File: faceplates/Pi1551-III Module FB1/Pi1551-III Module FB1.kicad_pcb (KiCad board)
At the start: 2 copper layers, 100 x 100 mm, 8 parts, among them M1 Mounting, M2 Mounting, M3 Mounting, M4 Mounting

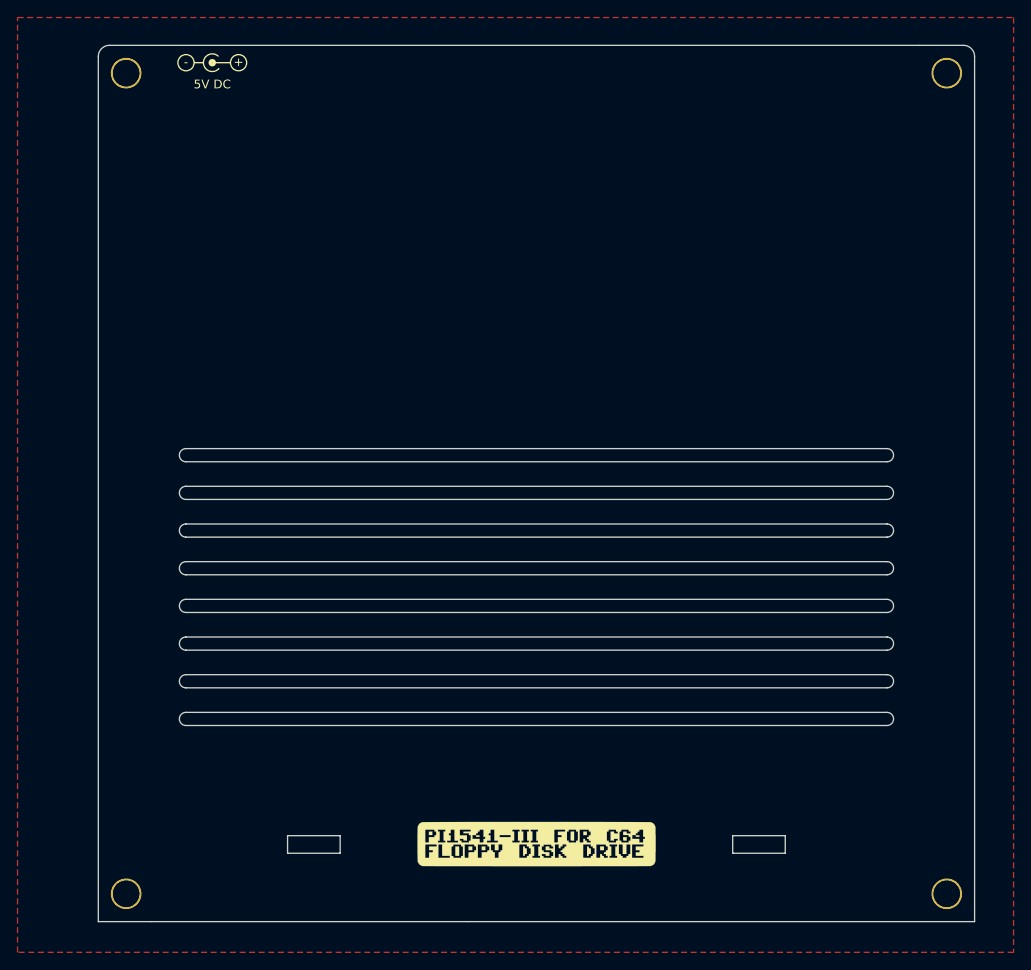
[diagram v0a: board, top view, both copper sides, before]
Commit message: upgrade to KiCad 9.0.7
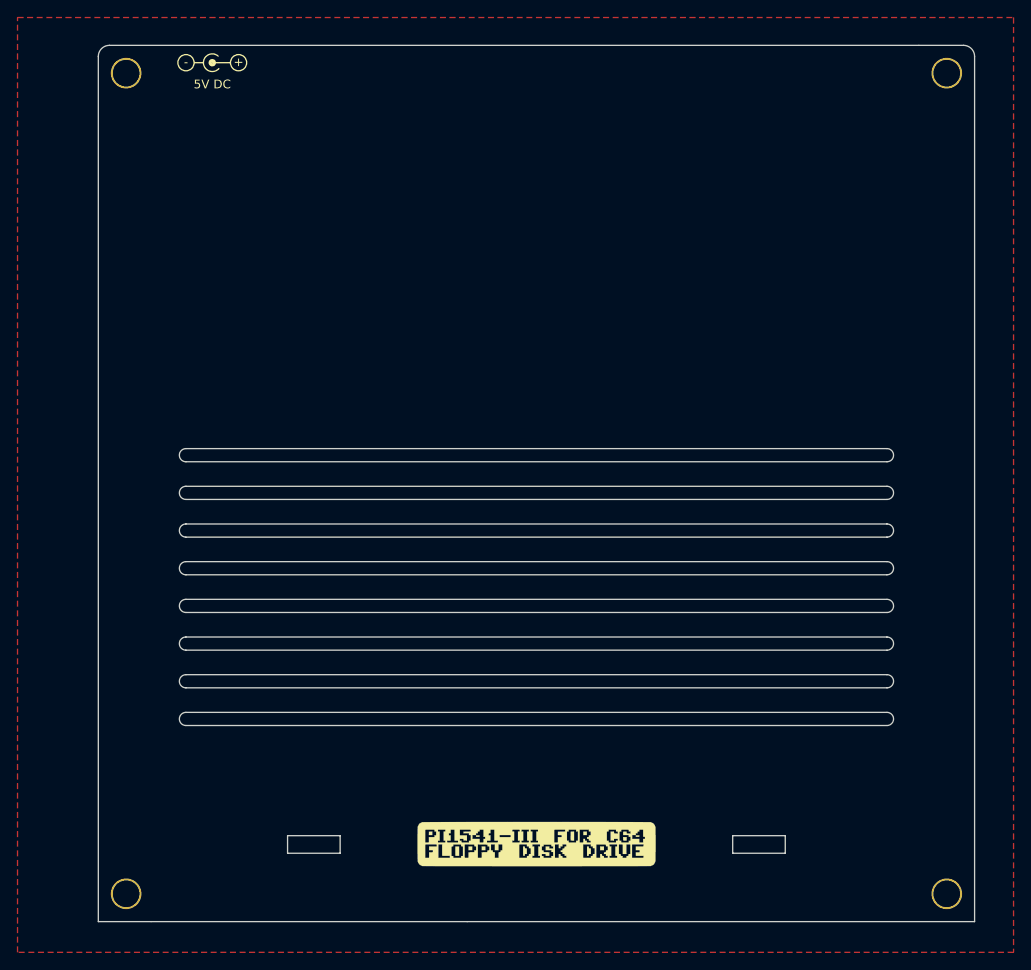
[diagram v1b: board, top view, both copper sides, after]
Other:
- net class Default removed
- net class Power removed
